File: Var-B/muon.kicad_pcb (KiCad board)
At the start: 2 copper layers, 20 x 13.5 mm, 9 parts, among them J1 HRO_TYPE-C-31-M-12, J2 SM04B-SRSS-TB, U1 TPD4E05U06DQA

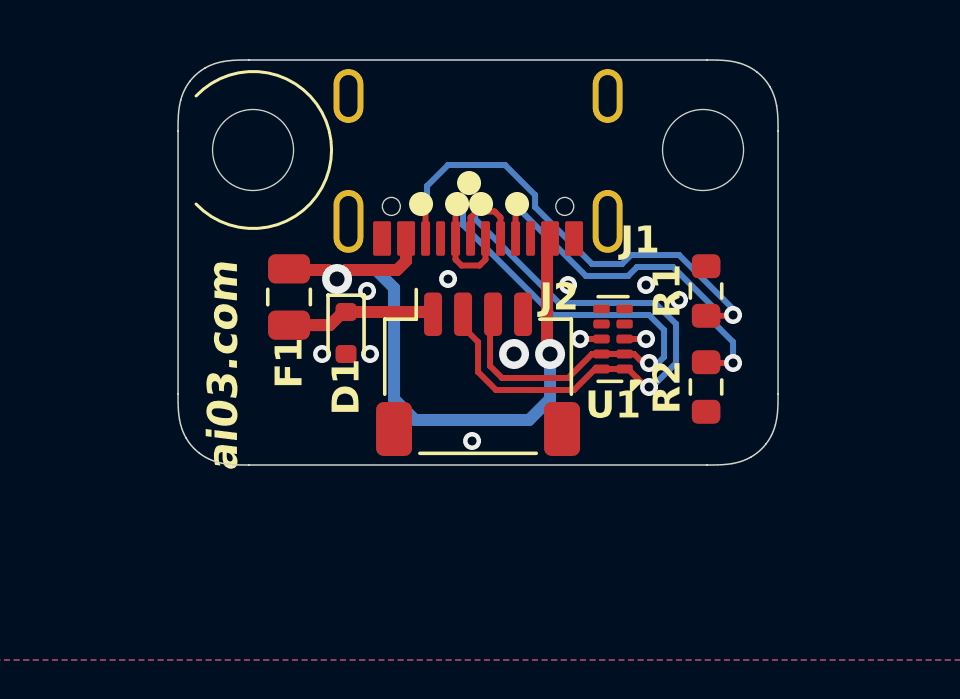
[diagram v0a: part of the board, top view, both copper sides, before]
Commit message: Adjust silkscreen
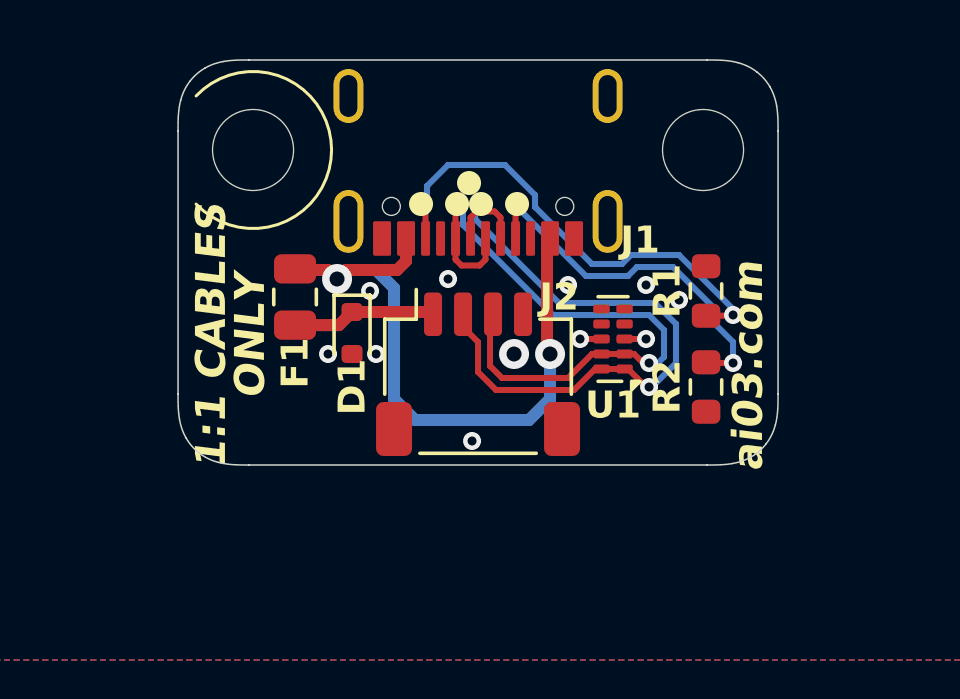
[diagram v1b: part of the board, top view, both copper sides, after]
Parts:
- moved D1 0.20 mm to (69.8, 59.1)
- moved F1 0.20 mm to (67.9, 57.9)
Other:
- board text added: "1:1 CABLES"
- board text added: "ONLY"

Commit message: Remove redundant silkscreen
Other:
- board text removed: "1:1 CABLES ONLY"
